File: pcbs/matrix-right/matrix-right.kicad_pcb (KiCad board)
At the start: 2 copper layers, 133.9 x 87.6 mm, 51 parts, among them J4 Conn_01x11, SW1 SW_Push, SW10 SW_Push, SW11 SW_Push, SW12 SW_Push, SW13 SW_Push, SW14 SW_Push, SW15 SW_Push, SW16 SW_Push, SW17 SW_Push, SW18 SW_Push, SW19 SW_Push, SW2 SW_Push, SW20 SW_Push, SW21 SW_Push, SW22 SW_Push, SW23 SW_Push, SW24 SW_Push, SW25 SW_Push, SW3 SW_Push, SW4 SW_Push, SW5 SW_Push, SW6 SW_Push, SW7 SW_Push, SW8 SW_Push, SW9 SW_Push

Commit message: Route the right matrix board
Same approach as the left board (36 vias). Replace a malformed R3 arc
whose mid point made it a near-full circle, which DRC flagged against
the board edge and a switch peg hole. DRC: no unconnected items or
clearance errors.

Co-Authored-By: Claude Opus 5.5 <noreply@anthropic.com>
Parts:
- moved D17 7.85 mm to (130.1, 96.9)
- moved D10 7.85 mm to (130.1, 77.9)
- moved D23 7.85 mm to (95.8, 117.7)
- moved D14 7.85 mm to (53.9, 84.1)
- moved D20 7.85 mm to (72.9, 99.4)
- moved D1 7.85 mm to (182.8, 69.7)
- moved D15 7.85 mm to (168.2, 102.6)
- moved D2 7.85 mm to (163.7, 69.7)
- moved D3 7.85 mm to (144.7, 64.0)
- moved D8 7.85 mm to (168.2, 83.6)
- moved D21 7.85 mm to (53.9, 103.2)
- moved D11 7.85 mm to (111.0, 76.0)
- moved D19 7.85 mm to (92.0, 96.9)
- moved D22 7.85 mm to (116.0, 116.0)
- moved D7 7.85 mm to (68.5, 70.3)
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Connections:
- J4 pad 1: /R0 -> /C3
- J4 pad 10: /C5 -> /C6
- J4 pad 11: /C6 -> /C5
- J4 pad 2: /R1 -> /C2
- J4 pad 3: /R2 -> /C1
- J4 pad 4: /R3 -> /C0
- J4 pad 5: /C0 -> /C4
- J4 pad 6: /C1 -> /R0
- J4 pad 7: /C2 -> /R1
- J4 pad 8: /C3 -> /R2
- J4 pad 9: /C4 -> /R3
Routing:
- net /R2: track 0.00 -> 146.5 mm, vias 0 -> 2
- net /R1: track 0.00 -> 125.8 mm
- net /C0: track 0.00 -> 125.1 mm, vias 0 -> 4
- net /R0: track 0.00 -> 121.7 mm
- net /R3: track 0.00 -> 114.8 mm, vias 0 -> 2
- net /C6: track 0.00 -> 114.0 mm, vias 0 -> 5
- net /C1: track 0.00 -> 101.1 mm, vias 0 -> 4
- net /C3: track 0.00 -> 92.3 mm, vias 0 -> 5
- net /C5: track 0.00 -> 90.1 mm, vias 0 -> 5
- net /C2: track 0.00 -> 86.3 mm, vias 0 -> 4
- net /C4: track 0.00 -> 77.5 mm, vias 0 -> 5
- net Net-(D17-A): track 0.00 -> 6.73 mm
- net Net-(D10-A): track 0.00 -> 6.73 mm
- net Net-(D1-A): track 0.00 -> 6.73 mm
- net Net-(D8-A): track 0.00 -> 6.73 mm
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
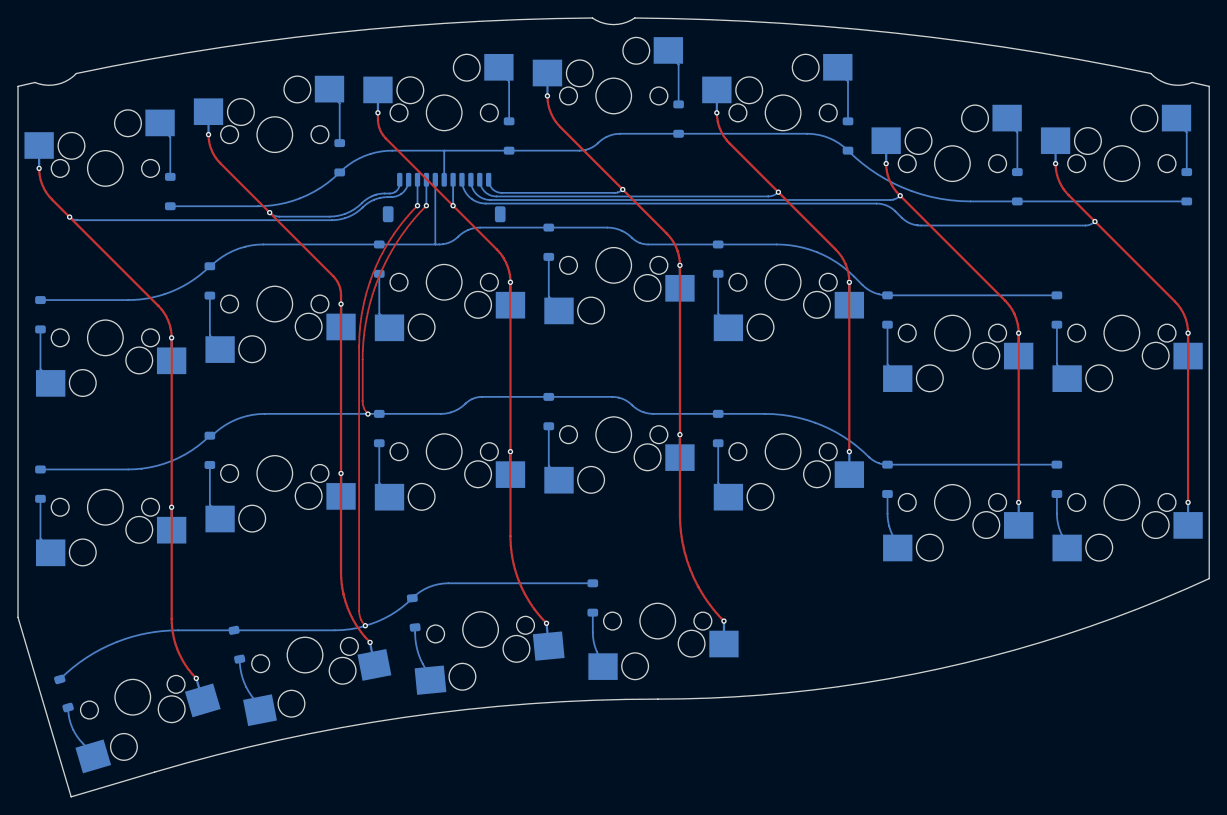
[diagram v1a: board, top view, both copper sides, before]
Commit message: Round the anode traces on the right matrix board
Redraw the socket-to-diode anode traces with arc bends instead of 45°
corners, and remove a dangling arc left on D15's anode. DRC: no
unconnected items, clearance errors, or dangling tracks.

Co-Authored-By: Claude Opus 5.5 <noreply@anthropic.com>
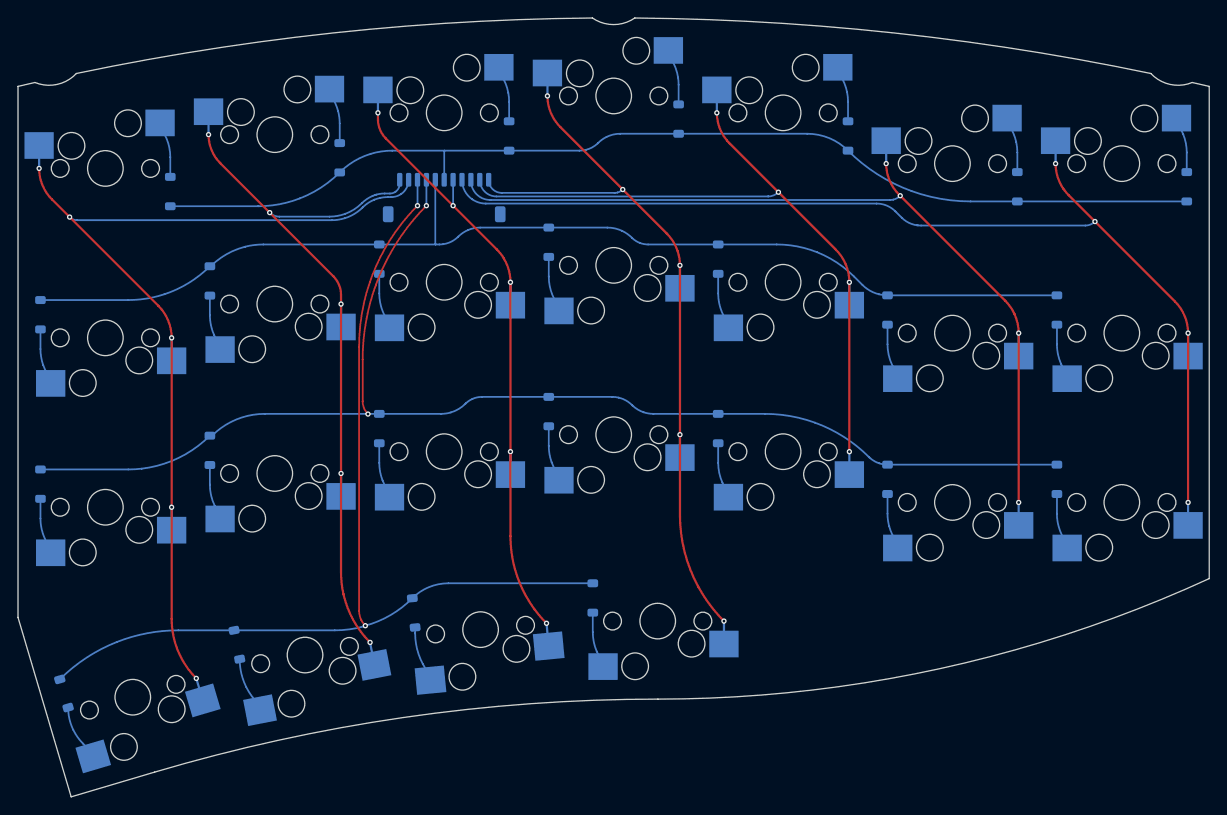
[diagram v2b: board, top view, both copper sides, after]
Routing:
- net Net-(D21-A): track 6.73 -> 4.69 mm
- net Net-(D15-A): track 6.49 -> 4.68 mm
- net Net-(D9-A): track 6.73 -> 5.85 mm

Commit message: Add the name silkscreen and teardrops to the matrix boards
Run add_matrix_silk.py on both boards and add teardrops. Every teardrop
stays at least 0.2 mm from copper on other nets (checked separately,
since DRC does not flag teardrops against other nets' pads). DRC: no
unconnected items or errors.

Co-Authored-By: Claude Opus 5.5 <noreply@anthropic.com>
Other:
- board text added: "optokbd matrix R v0.2.0 2026-10"
